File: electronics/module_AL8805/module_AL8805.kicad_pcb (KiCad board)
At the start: 2 copper layers, 26.8 x 13.6 mm, 14 parts, among them J1 Conn_01x03, J2 Conn_01x02, U1 AL8805

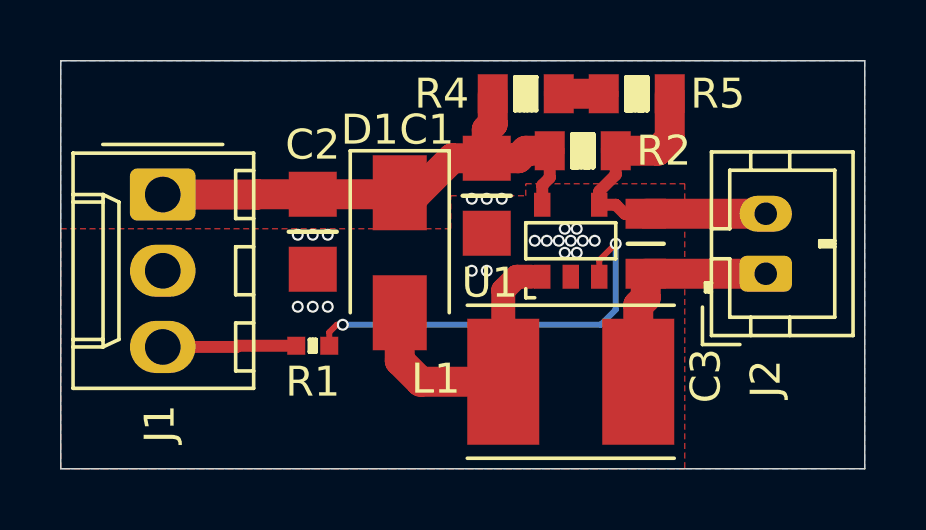
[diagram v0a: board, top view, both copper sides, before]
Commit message: added some power planes to ditribute power better
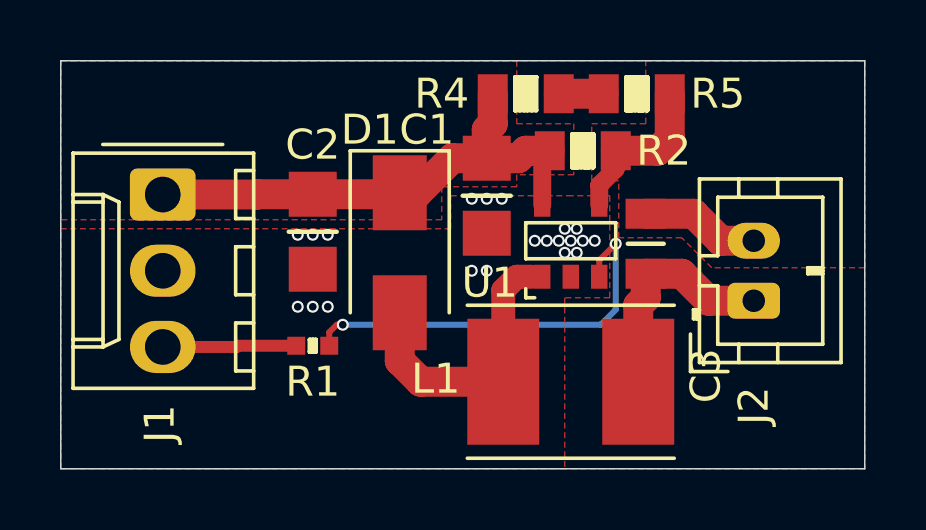
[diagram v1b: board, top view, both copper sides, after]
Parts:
- moved J2 0.98 mm to (162.1, 79.0)
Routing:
- net /LED+: track 11.2 -> 9.47 mm
- added copper zone on F.Cu, net /LED+
- added copper zone on F.Cu, net /Vin

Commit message: added output current label, silk movements, bit better component placement
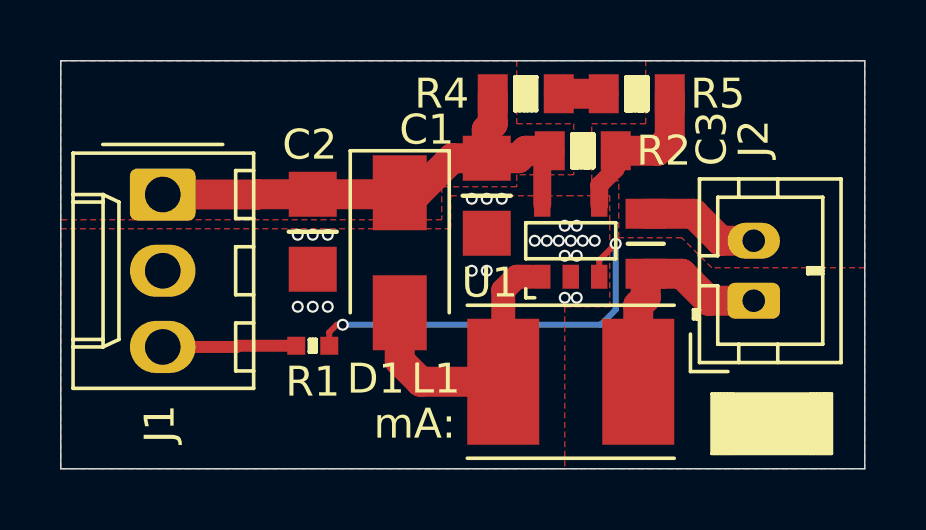
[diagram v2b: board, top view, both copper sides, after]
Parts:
- added N3: mA:, SquantorLabels:Label_Note_small, F.Cu at (159.7, 83.1)
- N1: value 20210309 -> 20210314
- moved N1 4.81 mm to (151.3, 77.2), turned to 270 degrees
- moved N2 2.91 mm to (147.5, 78.0), turned to 270 degrees
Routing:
- net /GND: vias 21 -> 23
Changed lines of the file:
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@@
     (thickness 1.6)
     (drawings 4)
-    (tracks 74)
+    (tracks 76)
     (zones 0)
-    (modules 14)
+    (modules 15)
     (nets 9)
   )
@@
     (add_net "Net-(R4-Pad1)")
   )
+  (module SquantorLabels:Label_Note_small (layer F.Cu)
+    (at 159.7 83.1)
+    (fp_text reference N3 (at -0.05 -2.3) (layer F.Fab) hide
+      (effects (font (size 1 1) (thickness 0.15)))
+    )
+    (fp_text value mA: (at -8.9 0) (layer F.SilkS)
+      (effects (font (size 1 1) (thickness 0.15)))
+    )
+    (fp_line (start 4.9 -1) (end 4.9 1) (layer F.SilkS) (width 0.1))
+    (fp_line (start 4.8 -1) (end 4.9 -1) (layer F.SilkS) (width 0.1))
+    (fp_line (start 4.8 1) (end 4.8 -1) (layer F.SilkS) (width 0.1))
+    (fp_line (start 4.7 -1) (end 4.7 1) (layer F.SilkS) (width 0.1))
+    (fp_line (start 4.6 1) (end 4.6 -1) (layer F.SilkS) (width 0.1))
+    (fp_line (start 4.5 -1) (end 4.5 1) (layer F.SilkS) (width 0.1))
+    (fp_line (start 4.4 1) (end 4.4 -1) (layer F.SilkS) (width 0.1))
+    (fp_line (start 4.3 -1) (end 4.3 1) (layer F.SilkS) (width 0.1))
+    (fp_line (start 1.7 1) (end 1.7 -1) (layer F.SilkS) (width 0.1))
+    (fp_line (start 1.6 -1) (end 1.6 1) (layer F.SilkS) (width 0.1))
+    (fp_line (start 1.5 1) (end 1.5 -1) (layer F.SilkS) (width 0.1))
+    (fp_line (start 1.4 -1) (end 1.4 1) (layer F.SilkS) (width 0.1))
+    (fp_line (start 1.3 1) (end 1.3 -1) (layer F.SilkS) (width 0.1))
+    (fp_line (start 1.2 -1) (end 1.2 1) (layer F.SilkS) (width 0.1))
+    (fp_line (start 1.1 1) (end 1.1 -1) (layer F.SilkS) (width 0.1))
+    (fp_line (start 1 1) (end 1 -1) (layer F.SilkS) (width 0.1))
+    (fp_line (start 5 1) (end 1 1) (layer F.SilkS) (width 0.1))
+    (fp_line (start 5 -1) (end 5 1) (layer F.SilkS) (width 0.1))
+    (fp_line (start 1 -1) (end 5 -1) (layer F.SilkS) (width 0.1))
+    (fp_line (start 2 0) (end 4 0) (layer F.SilkS) (width 2))
+  )
   (module SquantorIC:SOT25-diodesinc (layer F.Cu)
     (at 156 77)
@@
     (descr "JST PH series connector, B2B-PH-K (http://www.jst-mfg.com/product/pdf/eng/ePH.pdf), generated with kicad-footprint-generator")
     (tags "connector JST PH side entry")
-    (fp_text reference J2 (at -3.5 0 90) (layer F.SilkS)
-      (effects (font (size 1 1) (thickness 0.15)))
-    )
-    (fp_text value Conn_01x02 (at -3.6 0 90) (layer F.Fab)
+    (fp_text reference J2 (at 5.4 0 90) (layer F.SilkS)
+      (effects (font (size 1 1) (thickness 0.15)))
+    )
+    (fp_text value Conn_01x02 (at 5.3 -0.1 90) (layer F.Fab)
       (effects (font (size 1 1) (thickness 0.15)))
     )
@@
     (tags "Diode SMA (DO-214AC)")
     (attr smd)
-    (fp_text reference D1 (at -4.1 1 180) (layer F.SilkS)
-      (effects (font (size 1 1) (thickness 0.15)))
-    )
-    (fp_text value B240 (at -4.1 1 180) (layer F.Fab)
+    (fp_text reference D1 (at 4.2 0.8 180) (layer F.SilkS)
+      (effects (font (size 1 1) (thickness 0.15)))
+    )
+    (fp_text value B240 (at 4.2 0.8 180) (layer F.Fab)
       (effects (font (size 1 1) (thickness 0.15)))
     )
@@
     (tags "capacitor 0805")
     (attr smd)
-    (fp_text reference C3 (at 4.4 -2 90) (layer F.SilkS)
-      (effects (font (size 1 1) (thickness 0.15)))
-    )
-    (fp_text value 1u (at 4.4 -2 90) (layer F.Fab)
+    (fp_text reference C3 (at -3.5 -2.2 90) (layer F.SilkS)
+      (effects (font (size 1 1) (thickness 0.15)))
+    )
+    (fp_text value 1u (at -3.5 -2.1 90) (layer F.Fab)
       (effects (font (size 1 1) (thickness 0.15)))
     )
@@
     (tags "capacitor 1206&0805 dual footprint")
     (attr smd)
-    (fp_text reference C2 (at -2.9 0 180) (layer F.SilkS)
+    (fp_text reference C2 (at -2.9 0.1 180) (layer F.SilkS)
       (effects (font (size 1 1) (thickness 0.15)))
     )
@@
   )
   (module Symbol:OSHW-Symbol_6.7x6mm_SilkScreen (layer B.Cu)
-    (at 150.1 76.7 90)
+    (at 147.5 78 270)
     (descr "Open Source Hardware Symbol")
     (tags "Logo Symbol OSHW")
@@
   )
   (module SquantorLabels:Label_Generic (layer B.Cu)
-    (at 146.8 78.9 90)
+    (at 151.3 77.2 270)
     (descr "Label for general purpose use")
     (tags Label)
@@
       (effects (font (size 1 1) (thickness 0.15)) (justify mirror))
     )
-    (fp_text value 20210309 (at 0.8 0.1 90) (layer B.SilkS)
+    (fp_text value 20210314 (at 0.8 0.1 90) (layer B.SilkS)
       (effects (font (size 0.8 0.8) (thickness 0.15)) (justify mirror))
     )
@@
   (gr_line (start 165.8 71) (end 165.8 84.6) (layer Edge.Cuts) (width 0.05))
   (gr_line (start 139 71) (end 165.8 71) (layer Edge.Cuts) (width 0.05))
-  (via (at 155.8 77.4) (size 0.4) (drill 0.254) (layers F.Cu B.Cu) (net 1))
-  (via (at 156.2 77.4) (size 0.4) (drill 0.254) (layers F.Cu B.Cu) (net 1))
-  (via (at 155.8 76.6) (size 0.4) (drill 0.254) (layers F.Cu B.Cu) (net 1))
-  (via (at 156.2 76.6) (size 0.4) (drill 0.254) (layers F.Cu B.Cu) (net 1))
+  (via (at 155.8 77.5) (size 0.4) (drill 0.254) (layers F.Cu B.Cu) (net 1))
+  (via (at 156.2 77.5) (size 0.4) (drill 0.254) (layers F.Cu B.Cu) (net 1))
+  (via (at 155.8 76.5) (size 0.4) (drill 0.254) (layers F.Cu B.Cu) (net 1))
+  (via (at 156.2 76.5) (size 0.4) (drill 0.254) (layers F.Cu B.Cu) (net 1))
   (via (at 147.4 79.2) (size 0.4) (drill 0.254) (layers F.Cu B.Cu) (net 1))
   (via (at 147.9 79.2) (size 0.4) (drill 0.254) (layers F.Cu B.Cu) (net 1))
@@
   (via (at 155.2 77) (size 0.4) (drill 0.254) (layers F.Cu B.Cu) (net 1))
   (via (at 156.8 77) (size 0.4) (drill 0.254) (layers F.Cu B.Cu) (net 1))
+  (via (at 155.8 78.9) (size 0.4) (drill 0.254) (layers F.Cu B.Cu) (net 1))
+  (via (at 156.2 78.9) (size 0.4) (drill 0.254) (layers F.Cu B.Cu) (net 1))
   (segment (start 149.95 75.45) (end 150.85 75.45) (width 1) (layer F.Cu) (net 2))
   (segment (start 150.85 75.45) (end 152.05 74.25) (width 1) (layer F.Cu) (net 2))
@@
     (polygon
       (pts
-        (xy 155.8 78.9) (xy 155.8 84.6) (xy 139 84.6) (xy 139 76.6) (xy 152 76.6)
-        (xy 152 75.5) (xy 155.9 75.5) (xy 157.3 75.5) (xy 157.3 78.9)
+        (xy 155.8 79.2) (xy 155.8 84.6) (xy 139 84.6) (xy 139 76.6) (xy 152 76.6)
+        (xy 152 75.5) (xy 155.9 75.5) (xy 157.3 75.5) (xy 157.3 79.2)
       )
     )

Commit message: updated versionnumbers, added labels, review completed
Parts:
- N1: value 20210314 -> 20210315
